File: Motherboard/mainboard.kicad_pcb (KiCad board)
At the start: 4 copper layers, 35 x 35 mm, 48 parts, among them IC1 BMX160, J1 Conn_01x01, J2 10118194-0001LF, J28 Conn_01x01, J29 Conn_01x01, J3 Micro_SD_Card, J30 Conn_01x01, J4 xf2m-2415-1a, J5 XF2M-1015-1A, SW1 KMR231NG LFS, U1 RFM95W-915S2, U2 ATSAMD51G_TQFN48, U3 DRV8848, U4 TPS82740BSIPR, U5 DRV8848, U6 MAX708RESA-T, U8 RFM95W-915S2, X1 ANTENNA_U.FL, X2 ANTENNA_U.FL

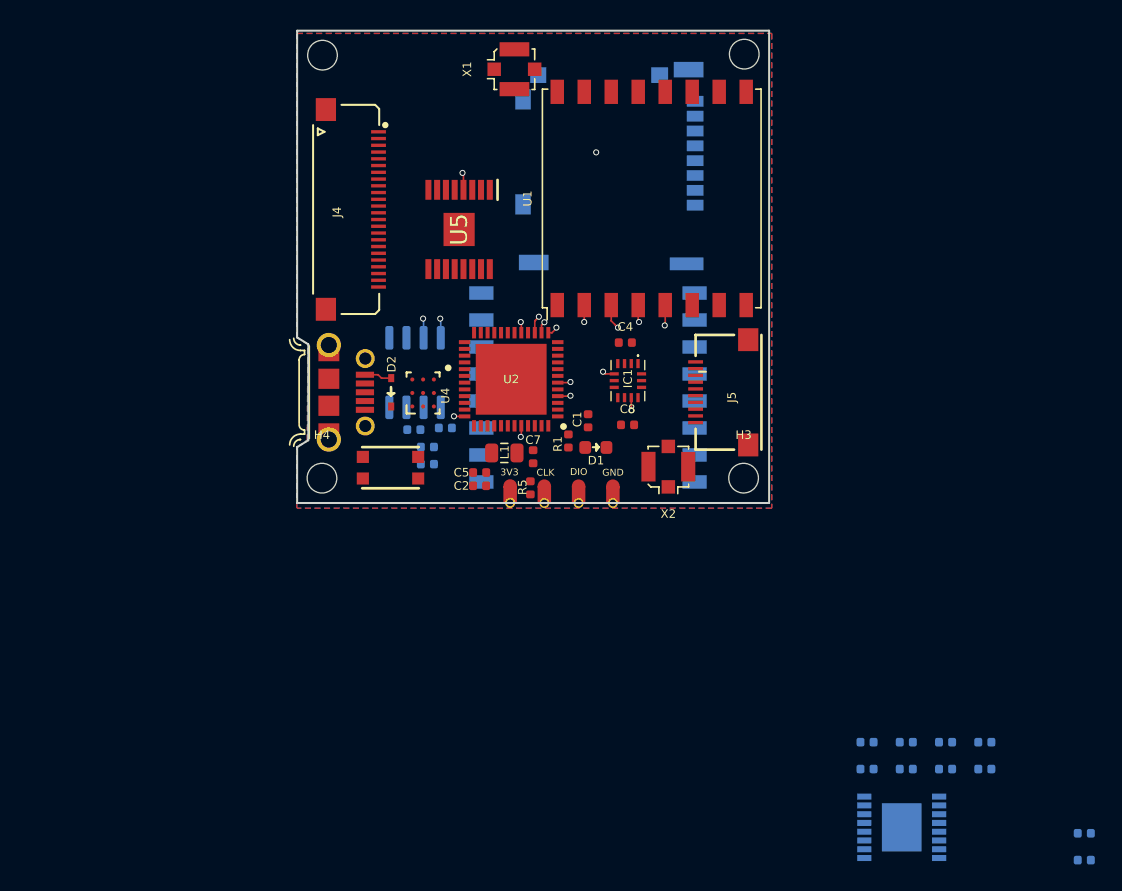
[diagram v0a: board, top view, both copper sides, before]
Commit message: updated top layer PCB layout
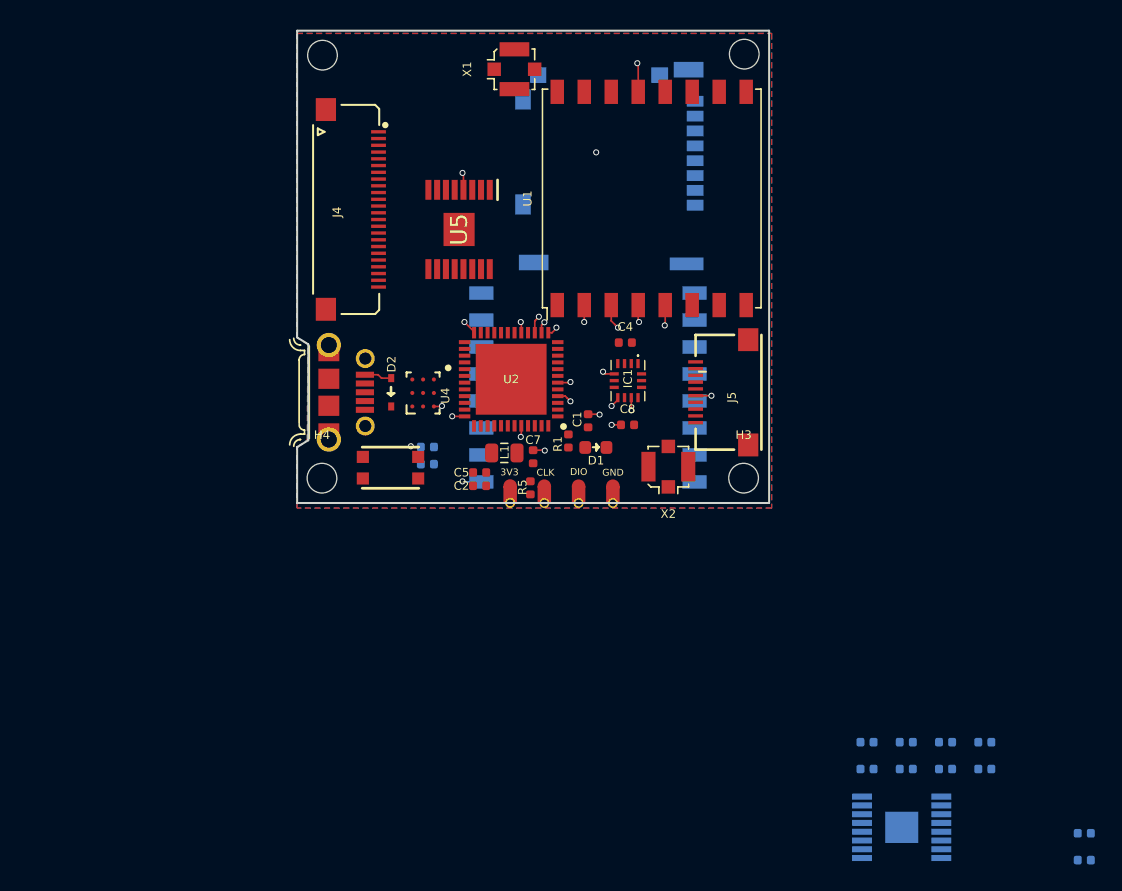
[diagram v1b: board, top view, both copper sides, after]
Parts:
- removed C3: 1uF, Capacitor_SMD:C_0402_1005Metric
- removed R3: 10K, Resistor_SMD:R_0402_1005Metric
- removed U6: MAX708RESA-T, Package_SO:SO-8_3.9x4.9mm_P1.27mm
- U3: footprint Package_SO:TSSOP-16-1EP_4.4x5mm_P0.65mm -> KiCAD Libraries:SOP65P640X120-17N
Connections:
- U3 pad 2: MINX_1 -> MOX_1
- U3 pad 4: MINX_2 -> MOX_2
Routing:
- net CS_CAM: track 0.00 -> 26.0 mm, vias 0 -> 2
- net +3V3: track 5.25 -> 11.5 mm, vias 6 -> 12
- net GND: track 2.88 -> 2.18 mm

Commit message: updated placement of H-bridges, flat flex connector, and additional wirings
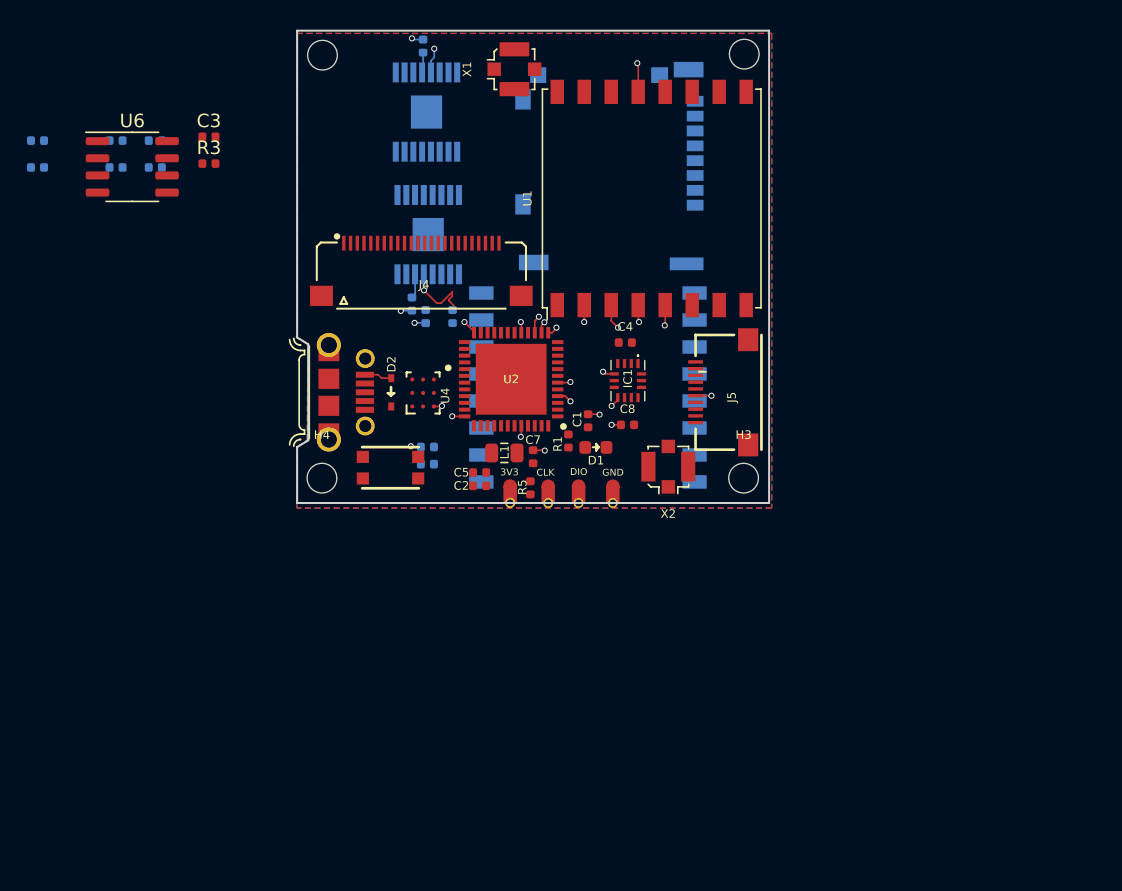
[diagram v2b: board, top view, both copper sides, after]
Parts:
- added C3: 1uF, Capacitor_SMD:C_0402_1005Metric, F.Cu at (75.2, 81.9)
- added R3: 10K, Resistor_SMD:R_0402_1005Metric, F.Cu at (75.2, 83.9)
- added U6: MAX708RESA-T, Package_SO:SO-8_3.9x4.9mm_P1.27mm, F.Cu at (69.5, 84.1)
- U5: moved to B.Cu
- moved C11 75.9 mm to (62.5, 82.2)
- moved C14 75.9 mm to (68.3, 84.2)
- moved C9 75.9 mm to (62.5, 84.2)
- moved R6 75.9 mm to (71.2, 84.2)
- moved R7 75.9 mm to (68.3, 82.2)
- moved R8 75.9 mm to (71.2, 82.2)
- moved C10 64.4 mm to (91.1, 75.2), turned to 90 degrees
- moved U3 63.6 mm to (91.3, 80.1), turned to 90 degrees
- moved C12 63.3 mm to (91.3, 95.2), turned to 270 degrees
- moved R4 60.5 mm to (93.2, 95.2), turned to 270 degrees
- moved C13 48.9 mm to (90.2, 94.3), turned to 90 degrees
- moved J4 4.04 mm to (90.9, 89.8), turned to 0 degrees
- moved U5 2.32 mm to (91.4, 89.2)
- moved J28 0.29 mm to (100.3, 107.7)
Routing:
- net Net-(IC1-Pad10): track 36.4 -> 0.00 mm, vias 2 -> 0
- net (no net): track 9.53 -> 0.00 mm
- net GND: track 2.18 -> 10.5 mm, vias 2 -> 6
- net MINX_2: track 6.59 -> 0.00 mm, vias 1 -> 0
- net Net-(C13-Pad2): track 0.00 -> 1.82 mm
- net Net-(C10-Pad1): track 0.00 -> 1.50 mm

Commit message: updated wiring on top layer, added CS_IMU net
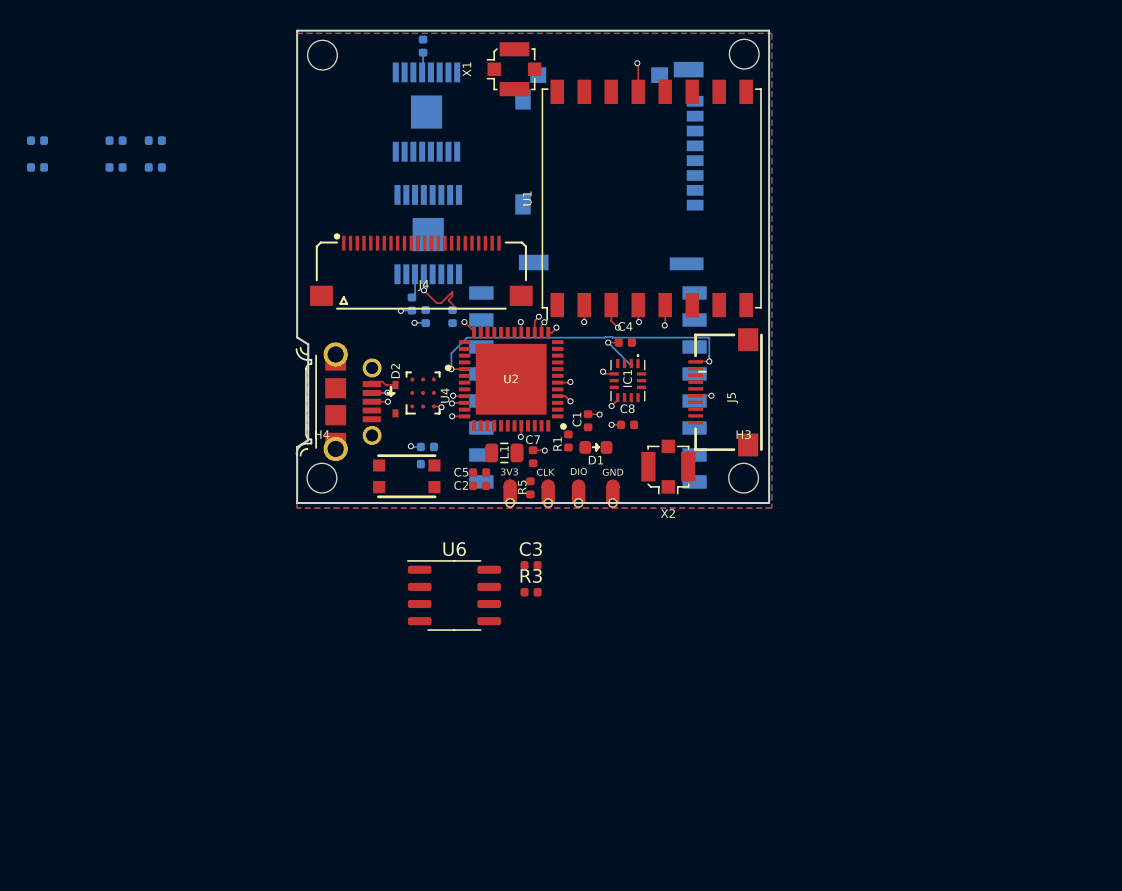
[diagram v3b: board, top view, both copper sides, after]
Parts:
- moved C3 39.7 mm to (99.1, 113.7)
- moved R3 39.7 mm to (99.1, 115.7)
- moved U6 39.7 mm to (93.4, 115.9)
- moved SW1 1.36 mm to (89.9, 107.1), turned to 180 degrees
- moved J2 0.86 mm to (84.6, 101.5)
- moved D2 0.60 mm to (89.0, 101.3)
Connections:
- U2 pad 27: Net-(U2-Pad27) -> CS_IMU
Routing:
- net EN_CAM: track 0.00 -> 24.6 mm, vias 0 -> 2
- net CS_CAM: track 26.0 -> 2.26 mm
- net /USB-: track 0.00 -> 7.81 mm, vias 0 -> 2
- net /USB+: track 0.00 -> 6.95 mm, vias 0 -> 2
- net +3V3: track 11.5 -> 14.8 mm, vias 12 -> 13
- net GND: track 10.5 -> 7.74 mm, vias 6 -> 4

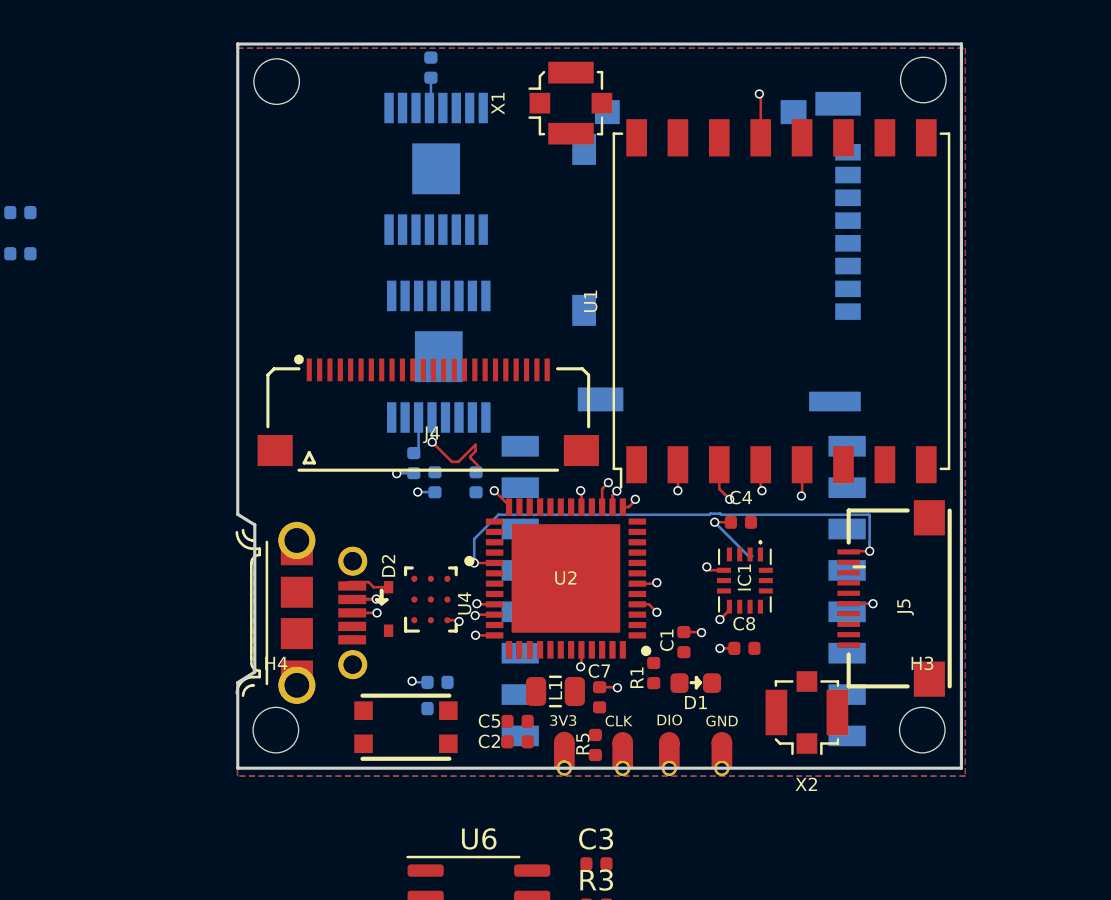
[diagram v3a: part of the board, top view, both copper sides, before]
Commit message: updating board outline to tentative design per @ellised discussion
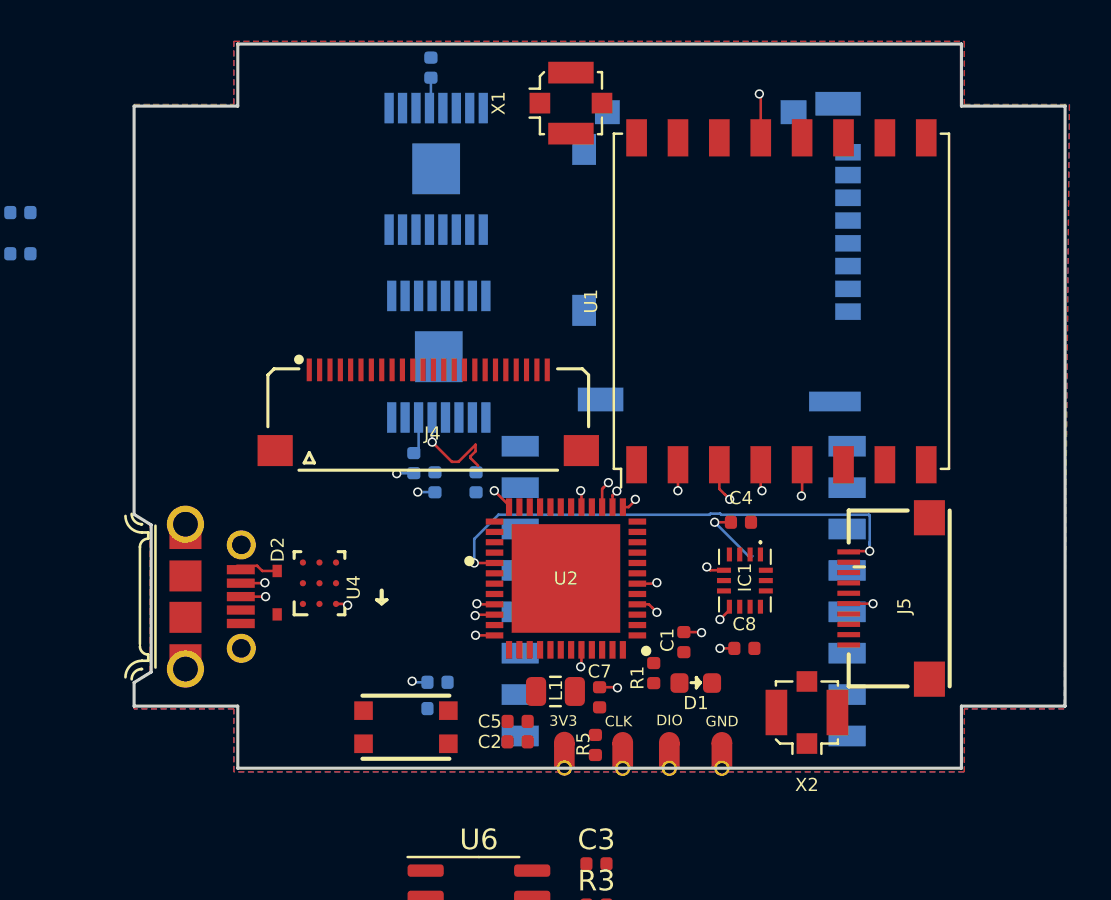
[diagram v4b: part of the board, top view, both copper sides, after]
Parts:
- removed H1, H2, H3, H4: MountingHole, MountingHole:MountingHole_2.2mm_M2
- moved D2 5.44 mm to (83.6, 100.6)
- moved J2 5.44 mm to (79.2, 100.7)
- moved U4 5.44 mm to (85.7, 100.1)
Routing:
- net /USB-: track 7.81 -> 6.99 mm
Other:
- board size 35 x 35 mm -> 45 x 35 mm

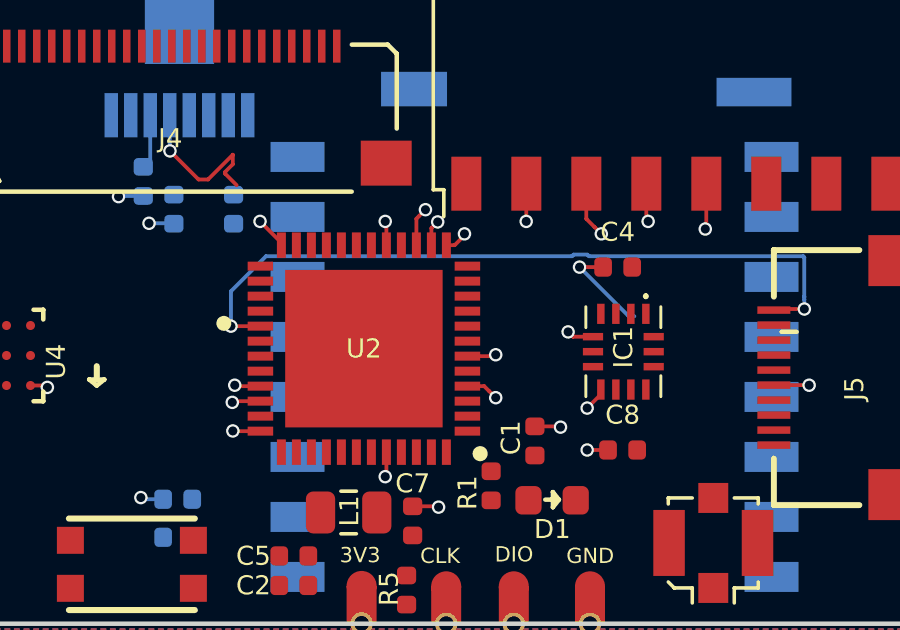
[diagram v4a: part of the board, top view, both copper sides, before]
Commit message: updated wiring on top layer, added CS_IMU connections
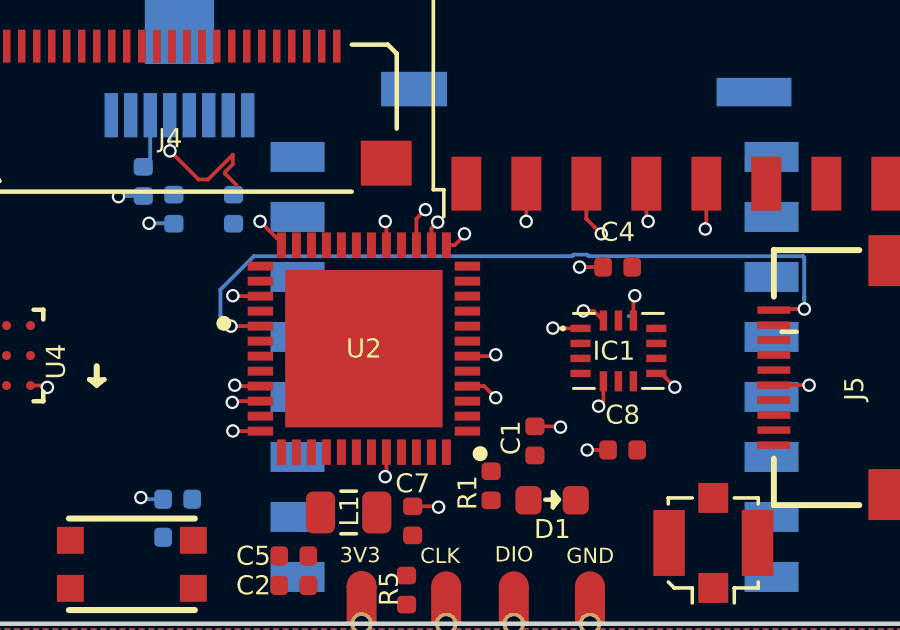
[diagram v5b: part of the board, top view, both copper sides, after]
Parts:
- moved IC1 0.17 mm to (106.1, 99.9), turned to 180 degrees
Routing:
- net CS_IMU: track 0.00 -> 15.2 mm, vias 0 -> 2
- net MISO: track 6.67 -> 11.6 mm, vias 2 -> 3
- net MOSI: track 7.49 -> 11.1 mm, vias 2 -> 3
- net +3V3: track 14.8 -> 12.5 mm
- net EN_CAM: track 24.6 -> 25.1 mm
